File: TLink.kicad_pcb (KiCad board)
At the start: 2 copper layers, 15.2 x 26.2 mm, 18 parts, among them J1 ZH_01x06, J2 TYPEC-304S-ACP16, P1 RT9013-33GB, SW1 SW_SPST, SW2 SW_SPST, U1 CH549F

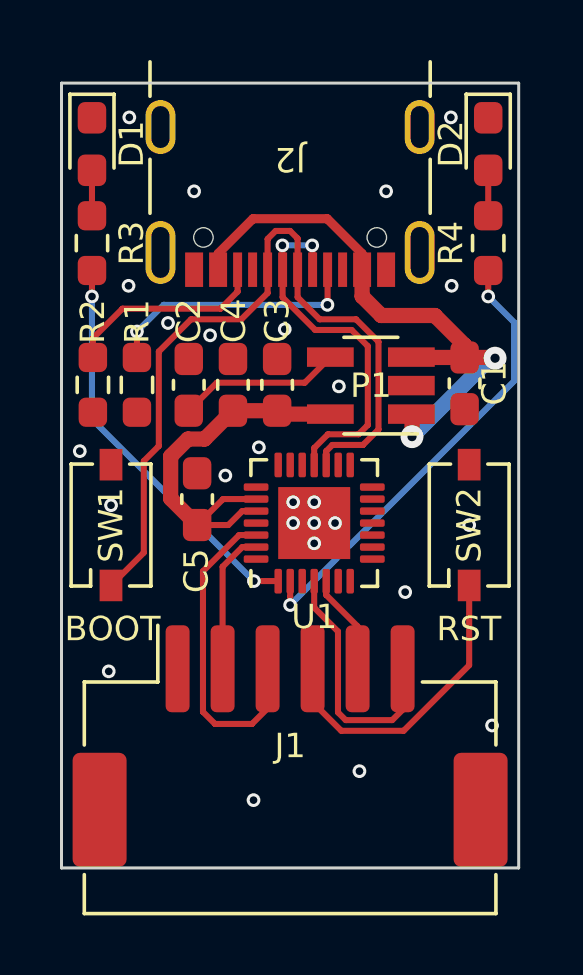
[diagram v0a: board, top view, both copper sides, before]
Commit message: TLink v1.1 For ARM/RISC-V
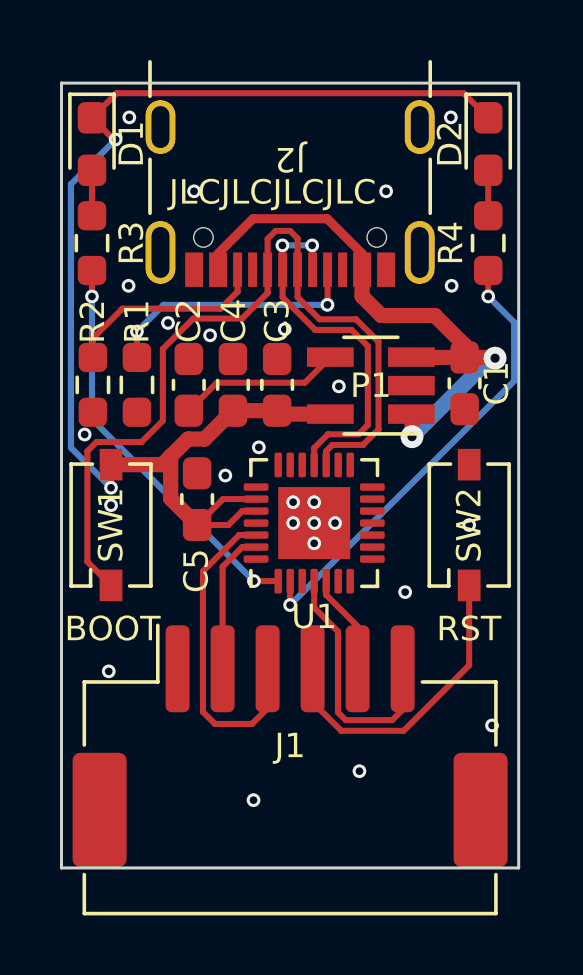
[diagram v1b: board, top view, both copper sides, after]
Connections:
- D1 pad 1: GND -> +3V3
- D2 pad 1: GND -> +3V3
- SW1 pad 2: GND -> +3V3
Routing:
- net +3V3: track 13.1 -> 43.8 mm, vias 0 -> 2
- net /DP: track 26.6 -> 28.1 mm
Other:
- board text added: "JLCJLCJLCJLC"
- board text added: "v1.1"
- board text removed: "v1.0"
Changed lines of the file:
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@@
       (net 13 "/DP") (pinfunction "A") (pintype "passive"))
     (pad "2" smd rect (at 2.013 0 90) (size 1.054 0.76) (layers "F.Cu" "F.Paste" "F.Mask")
-      (net 2 "GND") (pinfunction "B") (pintype "passive"))
+      (net 4 "+3V3") (pinfunction "B") (pintype "passive"))
     (model "D:/library/KiCad/Tenire.3D/Button_Turtle_3x4x2_180.stp"
       (offset (xyz 0 0 0))
@@
       (stroke (width 0.1) (type solid)) (layer "F.Fab"))
     (pad "1" smd roundrect (at -0.875 0 270) (size 1.05 0.95) (layers "F.Cu" "F.Paste" "F.Mask") (roundrect_rratio 0.25)
-      (net 2 "GND") (pinfunction "K") (pintype "passive"))
+      (net 4 "+3V3") (pinfunction "K") (pintype "passive"))
     (pad "2" smd roundrect (at 0.875 0 270) (size 1.05 0.95) (layers "F.Cu" "F.Paste" "F.Mask") (roundrect_rratio 0.25)
       (net 5 "Net-(D1-A)") (pinfunction "A") (pintype "passive"))
@@
     (property "ki_keywords" "capacitor cap")
     (attr smd)
-    (fp_text reference "C1" (at 0 -0.9906 90) (layer "F.SilkS")
+    (fp_text reference "C1" (at 0 -1.0668 90) (layer "F.SilkS")
         (effects (font (size 0.8128 0.8128) (thickness 0.15)))
     )
@@
     (property "ki_keywords" "LED diode light-emitting-diode")
     (attr smd)
-    (fp_text reference "D2" (at 0 1.2446 -90) (layer "F.SilkS")
+    (fp_text reference "D2" (at 0 1.27 -90) (layer "F.SilkS")
         (effects (font (size 0.8128 0.8128) (thickness 0.15)))
     )
@@
       (stroke (width 0.1) (type solid)) (layer "F.Fab"))
     (pad "1" smd roundrect (at -0.875 0 270) (size 1.05 0.95) (layers "F.Cu" "F.Paste" "F.Mask") (roundrect_rratio 0.25)
-      (net 2 "GND") (pinfunction "K") (pintype "passive"))
+      (net 4 "+3V3") (pinfunction "K") (pintype "passive"))
     (pad "2" smd roundrect (at 0.875 0 270) (size 1.05 0.95) (layers "F.Cu" "F.Paste" "F.Mask") (roundrect_rratio 0.25)
       (net 6 "Net-(D2-A)") (pinfunction "A") (pintype "passive"))
@@
     (effects (font (size 0.8128 0.8128) (thickness 0.1016)) (justify left bottom mirror))
   )
-  (gr_text "v1.0" (at 148.8186 93.1926 90) (layer "B.SilkS")
+  (gr_text "v1.1" (at 148.8186 93.1926 90) (layer "B.SilkS")
     (effects (font (size 1.27 1.27) (thickness 0.15875)) (justify left bottom mirror))
   )
   (gr_text "Tenire" (at 152.2984 84.7344 90) (layer "B.SilkS")
     (effects (font (size 2.54 2.54) (thickness 0.3175)) (justify left bottom mirror))
+  )
+  (gr_text "JLCJLCJLCJLC" (at 148.5392 75.2602) (layer "F.SilkS")
+    (effects (font (size 0.8128 0.8128) (thickness 0.1016)) (justify left bottom))
   )
   (gr_text "BOOT" (at 145.0594 89.8144) (layer "F.SilkS")
@@
   (via (at 156.4132 88.1126) (size 0.4572) (drill 0.254) (layers "F.Cu" "B.Cu") (net 2))
   (via (at 154.2034 81.2546) (size 0.4572) (drill 0.254) (layers "F.Cu" "B.Cu") (net 2))
-  (via (at 145.5674 83.4136) (size 0.4572) (drill 0.254) (layers "F.Cu" "B.Cu") (net 2))
+  (via (at 145.729833 82.859294) (size 0.4572) (drill 0.254) (layers "F.Cu" "B.Cu") (net 2))
   (via (at 153.381 86.487) (size 0.4572) (drill 0.254) (layers "F.Cu" "B.Cu") (net 2))
   (via (at 148.508364 79.140964) (size 0.4572) (drill 0.254) (layers "F.Cu" "B.Cu") (free) (net 2))
@@
   (segment (start 153.0666 81.1328) (end 150.1331 81.1328) (width 0.2032) (layer "F.Cu") (net 3))
   (segment (start 153.9202 80.2792) (end 153.0666 81.1328) (width 0.2032) (layer "F.Cu") (net 3))
+  (segment (start 146.7944 71.4818) (end 158.3612 71.4818) (width 0.2032) (layer "F.Cu") (net 4))
   (segment (start 150.3445 85.0108) (end 149.479 85.8763) (width 0.2032) (layer "F.Cu") (net 4))
   (segment (start 152.2589 82.1792) (end 152.146 82.0663) (width 0.508) (layer "F.Cu") (net 4))
   (segment (start 149.1712 83.0102) (end 148.5976 83.5838) (width 0.508) (layer "F.Cu") (net 4))
   (segment (start 151.4435 85.4108) (end 150.983401 85.4108) (width 0.2032) (layer "F.Cu") (net 4))
+  (segment (start 146.7612 73.025) (end 146.6964 73.025) (width 0.2032) (layer "F.Cu") (net 4))
+  (segment (start 145.9738 72.3024) (end 146.7944 71.4818) (width 0.2032) (layer "F.Cu") (net 4))
   (segment (start 150.6728 82.0663) (end 149.7289 83.0102) (width 0.508) (layer "F.Cu") (net 4))
   (segment (start 148.5976 84.9949) (end 149.479 85.8763) (width 0.508) (layer "F.Cu") (net 4))
+  (segment (start 146.6088 83.8644) (end 146.6088 84.633297) (width 0.2032) (layer "F.Cu") (net 4))
+  (segment (start 148.317 83.8644) (end 146.6088 83.8644) (width 0.508) (layer "F.Cu") (net 4))
   (segment (start 153.9202 82.1792) (end 152.2589 82.1792) (width 0.508) (layer "F.Cu") (net 4))
+  (segment (start 158.3612 71.4818) (end 159.1818 72.3024) (width 0.2032) (layer "F.Cu") (net 4))
   (segment (start 148.5976 83.5838) (end 148.5976 84.9949) (width 0.508) (layer "F.Cu") (net 4))
   (segment (start 150.517901 85.8763) (end 149.479 85.8763) (width 0.2032) (layer "F.Cu") (net 4))
   (segment (start 151.4435 85.0108) (end 150.3445 85.0108) (width 0.2032) (layer "F.Cu") (net 4))
   (segment (start 149.7289 83.0102) (end 149.1712 83.0102) (width 0.508) (layer "F.Cu") (net 4))
+  (segment (start 146.6964 73.025) (end 145.9738 72.3024) (width 0.2032) (layer "F.Cu") (net 4))
   (segment (start 152.146 82.0663) (end 150.6728 82.0663) (width 0.508) (layer "F.Cu") (net 4))
   (segment (start 150.983401 85.4108) (end 150.517901 85.8763) (width 0.2032) (layer "F.Cu") (net 4))
+  (segment (start 148.5976 83.5838) (end 148.317 83.8644) (width 0.508) (layer "F.Cu") (net 4))
+  (via (at 146.6088 84.633297) (size 0.4572) (drill 0.254) (layers "F.Cu" "B.Cu") (net 4))
+  (via (at 146.7612 73.025) (size 0.4572) (drill 0.254) (layers "F.Cu" "B.Cu") (net 4))
+  (segment (start 145.272633 83.29713) (end 145.272633 74.513567) (width 0.2032) (layer "B.Cu") (net 4))
+  (segment (start 145.272633 74.513567) (end 146.7612 73.025) (width 0.2032) (layer "B.Cu") (net 4))
+  (segment (start 146.6088 84.633297) (end 145.272633 83.29713) (width 0.2032) (layer "B.Cu") (net 4))
   (segment (start 145.9738 74.0524) (end 145.9738 75.5669) (width 0.2032) (layer "F.Cu") (net 5))
   (segment (start 159.1818 74.0524) (end 159.1818 75.5669) (width 0.2032) (layer "F.Cu") (net 6))
@@
   (segment (start 148.3614 78.5368) (end 147.4724 79.4258) (width 0.2032) (layer "B.Cu") (net 12))
   (segment (start 153.987401 83.2068) (end 155.008494 83.2068) (width 0.2032) (layer "F.Cu") (net 13))
-  (segment (start 150.9525 79.0189) (end 149.2763 79.0189) (width 0.2032) (layer "F.Cu") (net 13))
-  (segment (start 151.8278 78.1436) (end 150.9525 79.0189) (width 0.2032) (layer "F.Cu") (net 13))
-  (segment (start 149.2763 79.0189) (end 148.2014 80.0938) (width 0.2032) (layer "F.Cu") (net 13))
+  (segment (start 150.9774 78.994) (end 149.350235 78.994) (width 0.2032) (layer "F.Cu") (net 13))
+  (segment (start 148.336 80.008235) (end 148.336 82.399365) (width 0.2032) (layer "F.Cu") (net 13))
   (segment (start 155.008494 83.2068) (end 155.5242 82.691094) (width 0.2032) (layer "F.Cu") (net 13))
-  (segment (start 151.8278 77.3654) (end 151.8278 78.1436) (width 0.2032) (layer "F.Cu") (net 13))
+  (segment (start 149.350235 78.994) (end 148.336 80.008235) (width 0.2032) (layer "F.Cu") (net 13))
   (segment (start 153.781 83.8733) (end 153.781 83.413201) (width 0.2032) (layer "F.Cu") (net 13))
+  (segment (start 145.8214 87.103) (end 146.6088 87.8904) (width 0.2032) (layer "F.Cu") (net 13))
   (segment (start 155.5242 82.691094) (end 155.5242 79.767306) (width 0.2032) (layer "F.Cu") (net 13))
   (segment (start 154.776294 79.0194) (end 153.563294 79.0194) (width 0.2032) (layer "F.Cu") (net 13))
@@
   (segment (start 153.563294 79.0194) (end 152.8278 78.283906) (width 0.2032) (layer "F.Cu") (net 13))
   (segment (start 155.5242 79.767306) (end 154.776294 79.0194) (width 0.2032) (layer "F.Cu") (net 13))
+  (segment (start 146.1262 83.1088) (end 145.8214 83.4136) (width 0.2032) (layer "F.Cu") (net 13))
+  (segment (start 145.8214 83.4136) (end 145.8214 87.103) (width 0.2032) (layer "F.Cu") (net 13))
+  (segment (start 151.8278 78.1436) (end 150.9774 78.994) (width 0.2032) (layer "F.Cu") (net 13))
   (segment (start 152.8278 76.323) (end 152.5778 76.073) (width 0.2032) (layer "F.Cu") (net 13))
   (segment (start 151.8278 76.3404) (end 151.8278 77.3654) (width 0.2032) (layer "F.Cu") (net 13))
   (segment (start 152.5778 76.073) (end 152.0952 76.073) (width 0.2032) (layer "F.Cu") (net 13))
-  (segment (start 148.2014 80.0938) (end 148.2014 83.2434) (width 0.2032) (layer "F.Cu") (net 13))
-  (segment (start 148.2014 83.2434) (end 147.701 83.7438) (width 0.2032) (layer "F.Cu") (net 13))
-  (segment (start 147.701 86.7982) (end 146.6088 87.8904) (width 0.2032) (layer "F.Cu") (net 13))
-  (segment (start 147.701 83.7438) (end 147.701 86.7982) (width 0.2032) (layer "F.Cu") (net 13))
+  (segment (start 148.336 82.399365) (end 147.626565 83.1088) (width 0.2032) (layer "F.Cu") (net 13))
+  (segment (start 151.8278 77.3654) (end 151.8278 78.1436) (width 0.2032) (layer "F.Cu") (net 13))
+  (segment (start 147.626565 83.1088) (end 146.1262 83.1088) (width 0.2032) (layer "F.Cu") (net 13))
   (segment (start 152.0952 76.073) (end 151.8278 76.3404) (width 0.2032) (layer "F.Cu") (net 13))
   (segment (start 152.8278 77.3654) (end 152.8278 76.323) (width 0.2032) (layer "F.Cu") (net 13))
